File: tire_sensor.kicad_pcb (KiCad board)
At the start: 4 copper layers, 33 x 26 mm, 30 parts, among them J1 Conn_02x05_Odd_Even, J2 U.FL, U2 DPS368, U3 LIS3DHTR, X1 32MHz, X2 32.768kHz

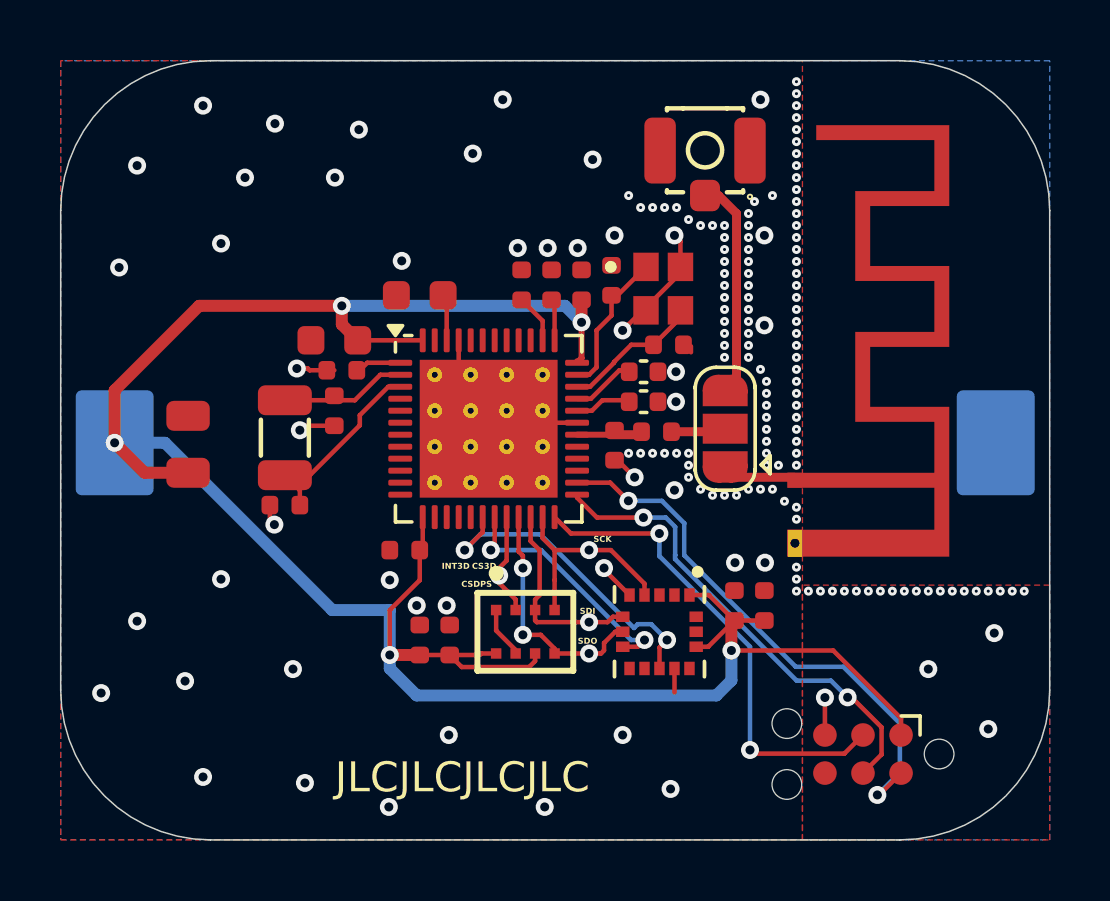
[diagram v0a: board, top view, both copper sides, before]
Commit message: Move ground plane to In1.Cu for RF
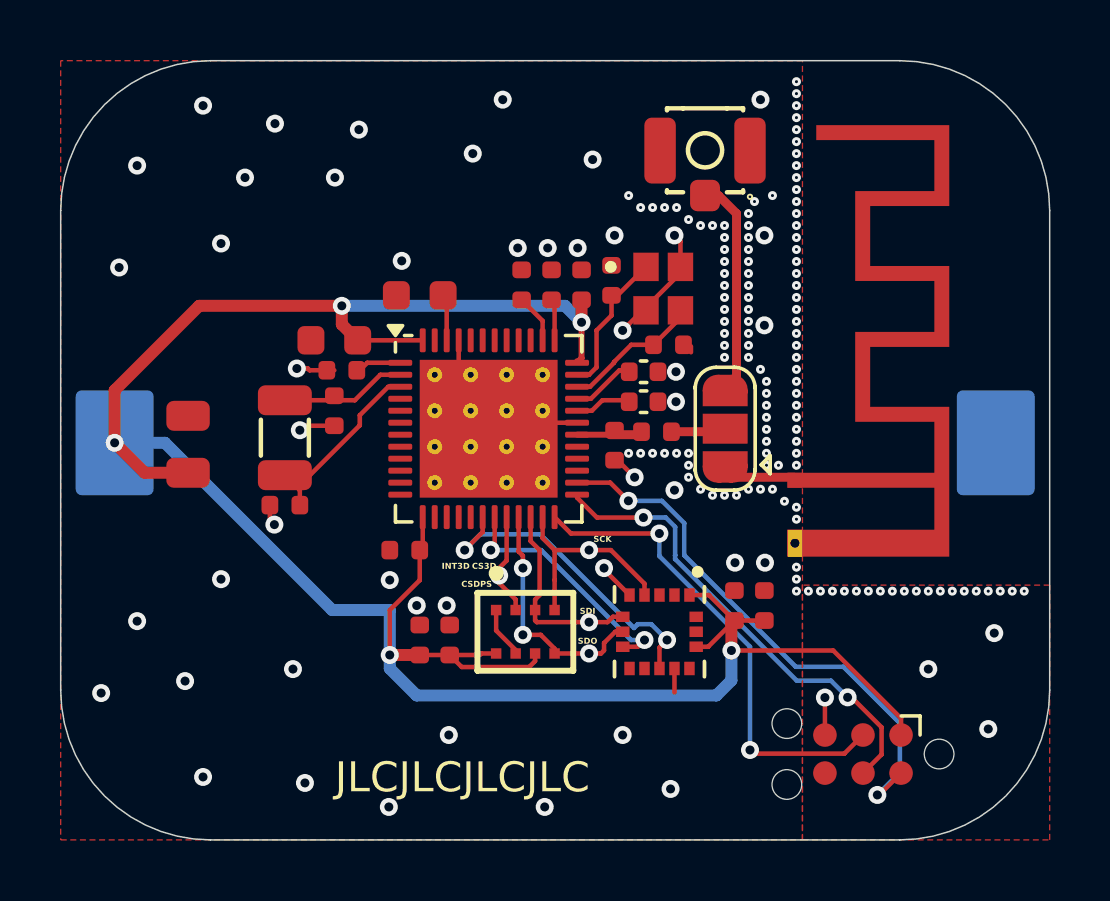
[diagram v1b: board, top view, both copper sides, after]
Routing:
- added copper zone on In1.Cu, net GND
- removed copper zone on B.Cu, net GND
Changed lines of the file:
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@@
 		(net_name "GND")
 		(locked yes)
-		(layer "B.Cu")
+		(layer "In1.Cu")
 		(hatch edge 0.5)
 		(connect_pads
@@
 		(polygon
 			(pts
-				(xy 155.81656 91.890685) (xy 155.81656 117.890685) (xy 188.81656 117.890685) (xy 188.81656 91.890685)
+				(xy 155.76656 91.990685) (xy 155.76656 117.990685) (xy 188.76656 117.990685) (xy 188.76656 91.990685)
 			)
 		)

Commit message: JCLPCB updated Crystal per stock, other fixes
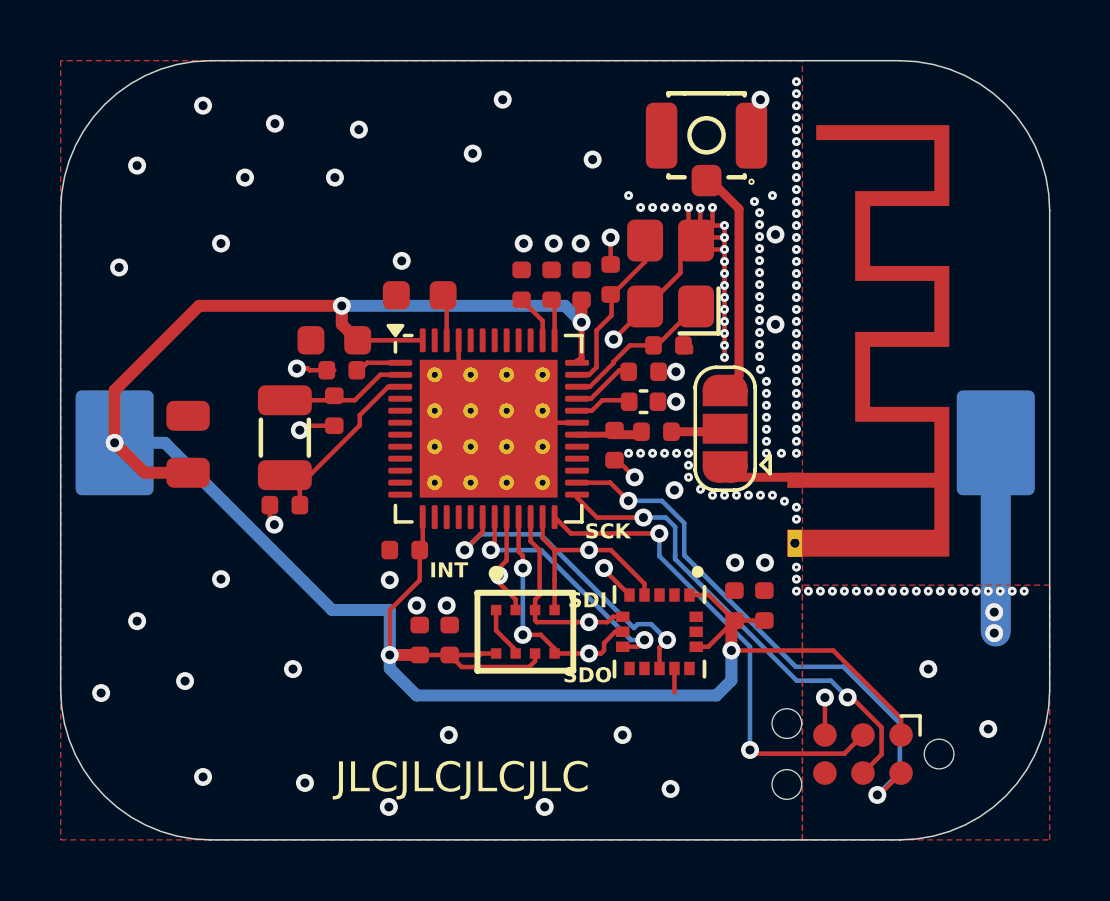
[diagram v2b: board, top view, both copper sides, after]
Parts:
- C7: footprint Capacitor_SMD:C_0402_1005Metric -> PCM_JLCPCB:C_0402
- X1: footprint footprints:XTAL_FA-128_32.0000MF20X-K3 -> PCM_JLCPCB:OSC-SMD_4P-L3.2-W2.5-BL_SIT8008BI
- moved X1 0.56 mm to (176.2, 99.0), turned to 90 degrees
- moved J2 0.50 mm to (177.4, 95.1)
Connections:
- AE1 pad 1: Net-(AE1-A) -> /RF
- J2 pad 1: Net-(J2-In) -> /RF
- JP1 pad 1: Net-(AE1-A) -> /RF
- JP1 pad 3: Net-(J2-In) -> /RF
- X1 pad 1: /XC2 -> /XC1
- X1 pad 3: /XC1 -> /XC2
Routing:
- net GND: track 20.1 -> 38.8 mm, vias 168 -> 166
- net /RF: track 1.75 -> 12.5 mm
- net Net-(J2-In): track 7.34 -> 0.00 mm
- net Net-(AE1-A): track 2.53 -> 0.00 mm
- net /XC2: track 4.90 -> 5.65 mm
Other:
- board text added: "INT"
- board text removed: "CS3D"
- board text removed: "CSDPS"
- board text removed: "INT3D"

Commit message: No uFL, LEDs, button
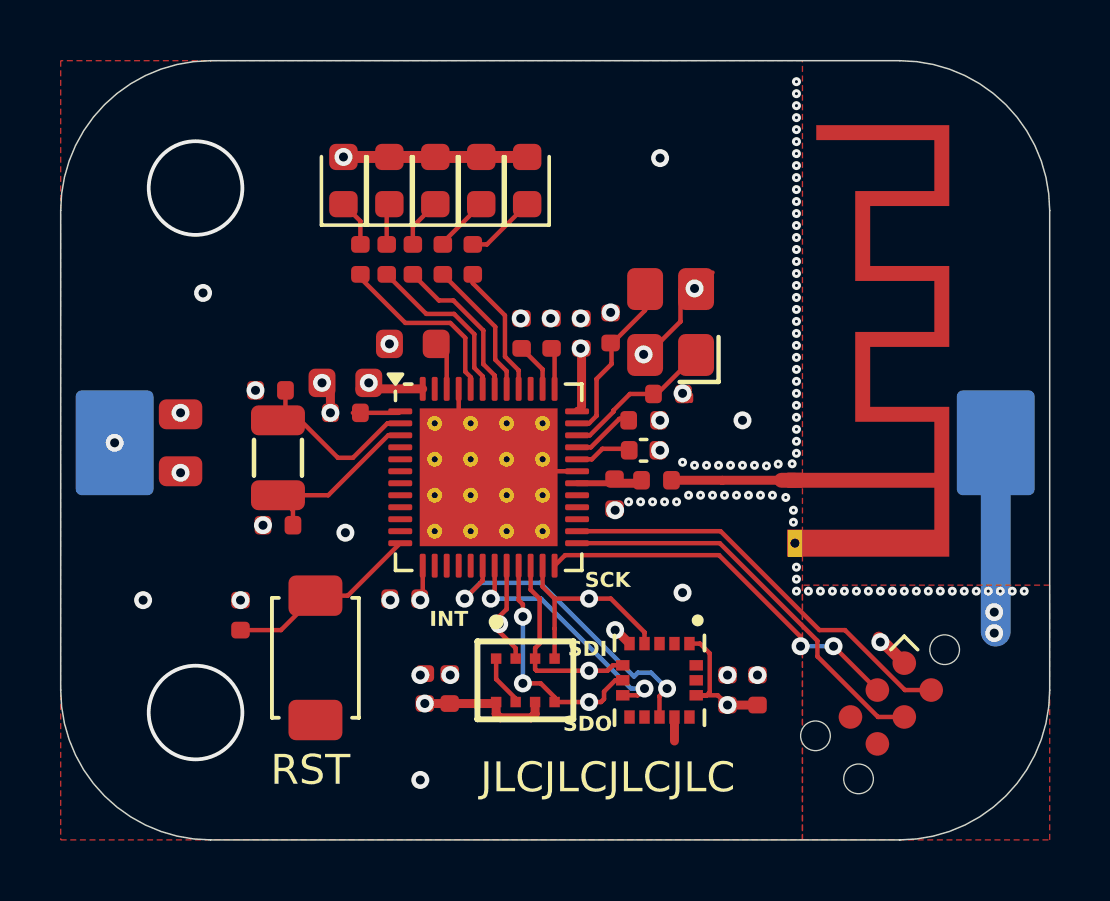
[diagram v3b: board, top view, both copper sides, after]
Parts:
- removed J2: U.FL, PCM_JLCPCB:IPEX-SMD_BWIPX-1-001E
- removed JP1: SolderJumper_3_Open, Jumper:SolderJumper-3_P1.3mm_Open_RoundedPad1.0x1.5mm
- added D1: LED, LED_SMD:LED_0603_1608Metric, F.Cu at (171.4, 95.9)
- added D2: LED, LED_SMD:LED_0603_1608Metric, F.Cu at (169.8, 95.9)
- added D3: LED, LED_SMD:LED_0603_1608Metric, F.Cu at (168.3, 95.9)
- added D4: LED, LED_SMD:LED_0603_1608Metric, F.Cu at (166.8, 95.9)
- added D5: LED, LED_SMD:LED_0603_1608Metric, F.Cu at (165.3, 95.9)
- added R1: 1kΩ, PCM_JLCPCB:R_0402, F.Cu at (169.6, 98.5)
- added R2: 1kΩ, PCM_JLCPCB:R_0402, F.Cu at (168.6, 98.5)
- added R3: 1kΩ, PCM_JLCPCB:R_0402, F.Cu at (167.6, 98.5)
- added R4: 1kΩ, PCM_JLCPCB:R_0402, F.Cu at (166.7, 98.5)
- added R5: 1kΩ, PCM_JLCPCB:R_0402, F.Cu at (165.8, 98.5)
- added R6: 10kΩ, PCM_JLCPCB:R_0402, F.Cu at (161.8, 110.4)
- added S1: Tactile Button, 160gf, PCM_JLCPCB:SW_TS-1088-AR02016, F.Cu at (164.3, 111.8)
- moved C16 2.83 mm to (178.1, 112.9)
- moved C17 2.83 mm to (179.1, 112.9)
- moved C11 2.24 mm to (162.8, 102.9), turned to 0 degrees
- moved J1 1.92 mm to (183.5, 113.3), turned to -135 degrees
- moved C10 1.64 mm to (167.6, 101.3)
- moved C19 1.63 mm to (168.0, 112.8)
- moved C13 1.62 mm to (172.2, 101.0)
- moved C14 1.62 mm to (171.2, 101.0)
- moved C2 1.62 mm to (174.2, 100.8)
- moved C6 1.62 mm to (175.3, 104.9)
- moved C7 1.62 mm to (175.3, 103.9)
- moved C8 1.62 mm to (173.2, 101.0)
- moved L1 1.62 mm to (175.7, 105.9)
- moved U2 1.62 mm to (171.3, 112.6)
- moved U3 1.62 mm to (175.8, 112.6)
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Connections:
- U1 pad 12: unconnected-(U1-P0.10-Pad12) -> /BTN
- U1 pad 40: unconnected-(U1-P0.28/AIN4-Pad40) -> /LED0
- U1 pad 41: unconnected-(U1-P0.29/AIN5-Pad41) -> /LED1
- U1 pad 42: unconnected-(U1-P0.30/AIN6-Pad42) -> /LED2
- U1 pad 43: unconnected-(U1-P0.31/AIN7-Pad43) -> /LED3
- U1 pad 44: unconnected-(U1-N.C.-Pad44) -> /LED4
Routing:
- net VDD_NRF: track 78.3 -> 24.0 mm, vias 5 -> 10
- net GND: track 38.8 -> 22.9 mm, vias 166 -> 113
- net /RF: track 12.5 -> 4.12 mm
- net /BTN: track 0.00 -> 6.53 mm
- net /LED4: track 0.00 -> 6.22 mm
- net /LED3: track 0.00 -> 5.69 mm
- net /LED2: track 0.00 -> 5.33 mm
- net /LED1: track 0.00 -> 4.70 mm
- net /SWDIO: track 18.5 -> 14.0 mm, vias 2 -> 0
- net /LED0: track 0.00 -> 4.45 mm
- net /nRESET: track 16.3 -> 13.0 mm
- net Net-(D1-K): track 0.00 -> 2.37 mm
- net /SWCLK: track 15.8 -> 13.6 mm, vias 2 -> 0
- net /P0.00/XL1: track 4.20 -> 6.18 mm
- net Net-(D2-K): track 0.00 -> 1.87 mm
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- added copper zone on In2.Cu, net VDD_NRF
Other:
- board text added: "RST"

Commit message: PCB tweaks
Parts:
- moved R1 4.12 mm to (173.6, 97.7), turned to 180 degrees
- moved R2 3.34 mm to (171.8, 97.7), turned to 180 degrees
- moved C11 2.60 mm to (165.1, 101.6), turned to -90 degrees
- moved R3 2.57 mm to (170.0, 97.7), turned to 180 degrees
- moved C12 2.40 mm to (163.8, 105.1), turned to -90 degrees
- moved C2 2.24 mm to (175.5, 99.0), turned to 0 degrees
- moved C9 2.19 mm to (166.9, 101.1), turned to 90 degrees
- moved X2 2.14 mm to (165.1, 104.4)
- moved C1 2.13 mm to (178.0, 102.0), turned to 90 degrees
- moved C4 2.12 mm to (165.9, 101.6), turned to 90 degrees
- moved R4 1.72 mm to (168.2, 97.7), turned to 0 degrees
- moved D1 1.65 mm to (173.0, 95.8)
- moved D2 1.65 mm to (171.5, 95.8)
- moved D3 1.65 mm to (170.0, 95.8)
- moved D4 1.65 mm to (168.4, 95.8)
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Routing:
- net GND: track 22.9 -> 14.5 mm, vias 113 -> 115
- net /P0.00/XL1: track 6.18 -> 3.62 mm
- net /P0.01/XL2: track 6.12 -> 3.88 mm
- net /LED0: track 4.45 -> 6.42 mm
- net VDD_NRF: track 24.0 -> 22.9 mm
- net Net-(D1-K): track 2.37 -> 1.55 mm
- net /LED4: track 6.22 -> 7.03 mm
- net /LED1: track 4.70 -> 5.40 mm
- net /XC1: track 5.11 -> 5.71 mm
- net /DEC1: track 1.60 -> 2.20 mm
- net /DEC2: track 1.89 -> 2.49 mm
